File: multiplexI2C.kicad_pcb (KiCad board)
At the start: 2 copper layers, 48.3 x 71.1 mm, 58 parts, among them J1 Screw_Terminal_01x04, J10 Screw_Terminal_01x02, J2 Screw_Terminal_01x04, J3 Screw_Terminal_01x04, J4 Screw_Terminal_01x04, J5 Screw_Terminal_01x04, J6 Screw_Terminal_01x04, J7 Screw_Terminal_01x04, J8 Screw_Terminal_01x04, J9 Conn_02x04_Top_Bottom, U1 PCA9548A, U4 AMS1117-3.3 SOT-223, U5 f411-RFM95W

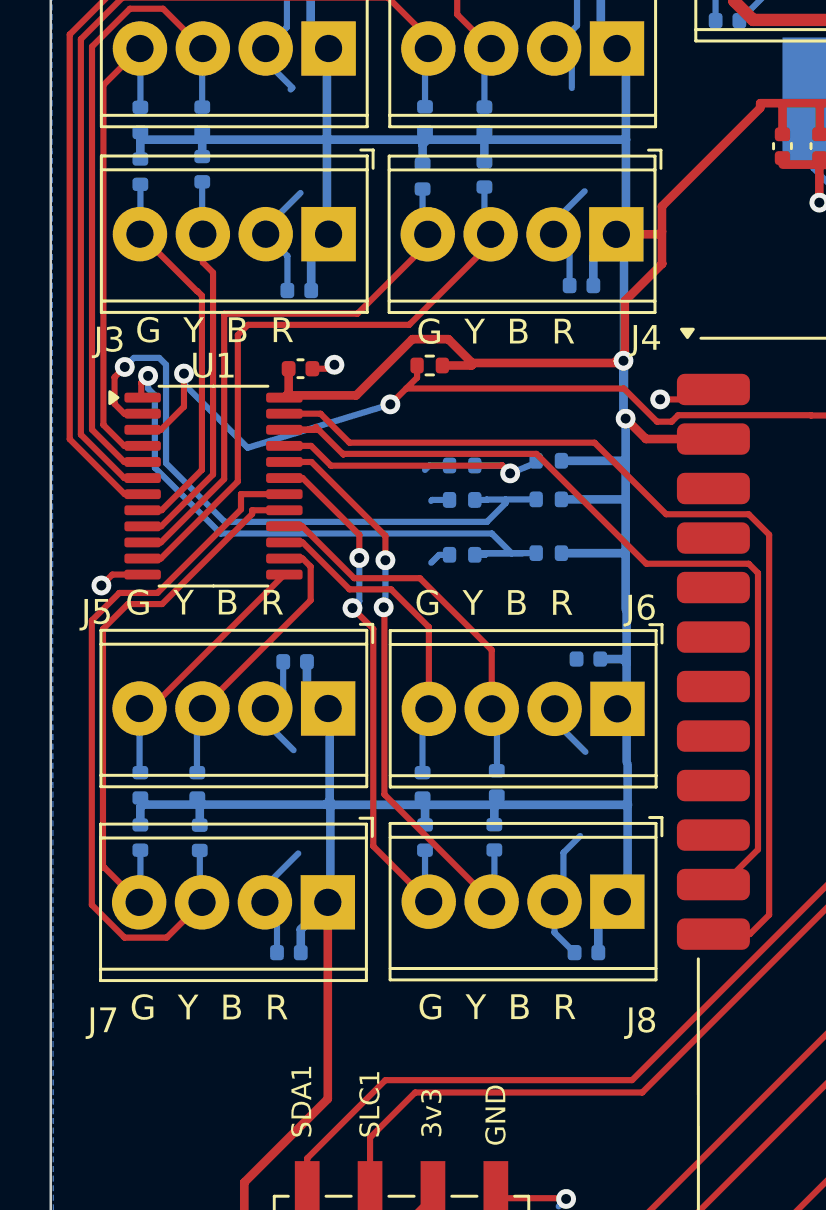
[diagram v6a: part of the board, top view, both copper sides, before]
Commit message: four sensor connectors flipped to the way they should be installed.
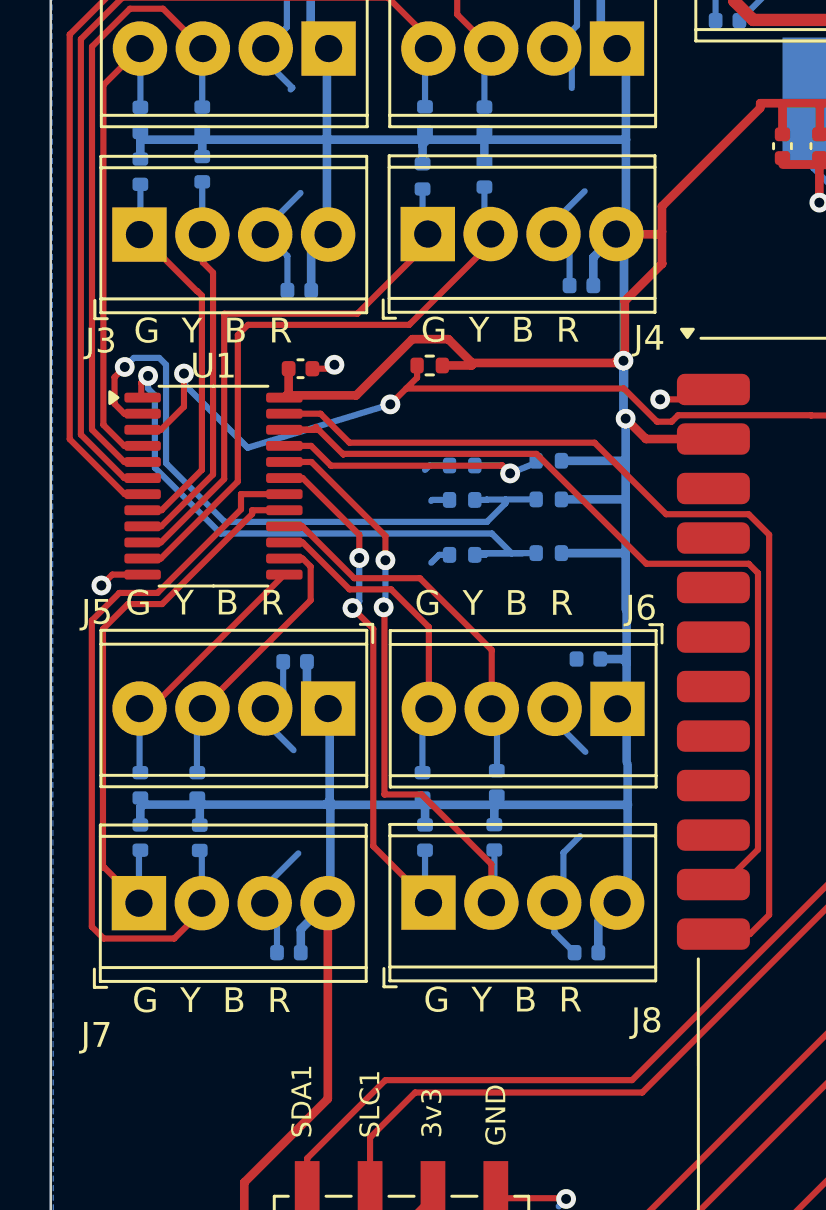
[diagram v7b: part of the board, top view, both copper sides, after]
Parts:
- moved J3 7.51 mm to (53.2, 41.0), turned to 0 degrees
- moved J8 7.50 mm to (64.9, 68.0), turned to 0 degrees
- moved J7 7.50 mm to (53.2, 68.0), turned to 0 degrees
- moved J4 7.49 mm to (64.8, 41.0), turned to 0 degrees
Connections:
- J3 pad 1: +3V3 -> /Connector_flipped2/SD
- J3 pad 2: GND -> /Connector_flipped2/SC
- J3 pad 3: /Connector2/SC -> GND
- J3 pad 4: /Connector2/SD -> +3V3
- J4 pad 1: +3V3 -> /Connector_flipped3/SD
- J4 pad 2: GND -> /Connector_flipped3/SC
- J4 pad 3: /Connector3/SC -> GND
- J4 pad 4: /Connector3/SD -> +3V3
- J7 pad 1: +3V3 -> /Connector_flipped6/SD
- J7 pad 2: GND -> /Connector_flipped6/SC
- J7 pad 3: /Connector6/SC -> GND
- J7 pad 4: /Connector6/SD -> +3V3
- J8 pad 1: +3V3 -> /Connector_flipped7/SD
- J8 pad 2: GND -> /Connector_flipped7/SC
- J8 pad 3: /Connector7/SC -> GND
- J8 pad 4: /Connector7/SD -> +3V3
- R14 pad 2: /Connector2/SC -> /Connector_flipped2/SC
- R15 pad 2: /Connector2/SD -> /Connector_flipped2/SD
- R16 pad 2: /Connector3/SC -> /Connector_flipped3/SC
- R17 pad 2: /Connector3/SD -> /Connector_flipped3/SD
- R22 pad 2: /Connector6/SC -> /Connector_flipped6/SC
- R23 pad 2: /Connector6/SD -> /Connector_flipped6/SD
- R24 pad 2: /Connector7/SC -> /Connector_flipped7/SC
- R25 pad 2: /Connector7/SD -> /Connector_flipped7/SD
- U1 pad 10: /Connector3/SD -> /Connector_flipped3/SD
- U1 pad 11: /Connector3/SC -> /Connector_flipped3/SC
- U1 pad 17: /Connector6/SD -> /Connector_flipped6/SD
- U1 pad 18: /Connector6/SC -> /Connector_flipped6/SC
- U1 pad 19: /Connector7/SD -> /Connector_flipped7/SD
- U1 pad 20: /Connector7/SC -> /Connector_flipped7/SC
- U1 pad 8: /Connector2/SD -> /Connector_flipped2/SD
- U1 pad 9: /Connector2/SC -> /Connector_flipped2/SC
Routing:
- net /Connector_flipped6/SC: track 0.00 -> 30.2 mm
- net /Connector6/SC: track 29.3 -> 0.00 mm
- net /Connector_flipped3/SC: track 0.00 -> 25.0 mm
- net /Connector3/SC: track 25.0 -> 0.00 mm
- net /Connector_flipped7/SC: track 0.00 -> 24.8 mm, vias 0 -> 2
- net /Connector7/SC: track 23.9 -> 0.00 mm, vias 2 -> 0
- net /Connector_flipped6/SD: track 0.00 -> 23.3 mm
- net /Connector6/SD: track 23.1 -> 0.00 mm
- net /Connector_flipped3/SD: track 0.00 -> 22.6 mm
- net /Connector3/SD: track 22.6 -> 0.00 mm
- net /Connector_flipped7/SD: track 0.00 -> 22.1 mm, vias 0 -> 2
- net /Connector7/SD: track 22.1 -> 0.00 mm, vias 2 -> 0
- net /Connector_flipped2/SC: track 0.00 -> 15.7 mm
- net /Connector2/SC: track 15.7 -> 0.00 mm
- net /Connector_flipped2/SD: track 0.00 -> 15.6 mm
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
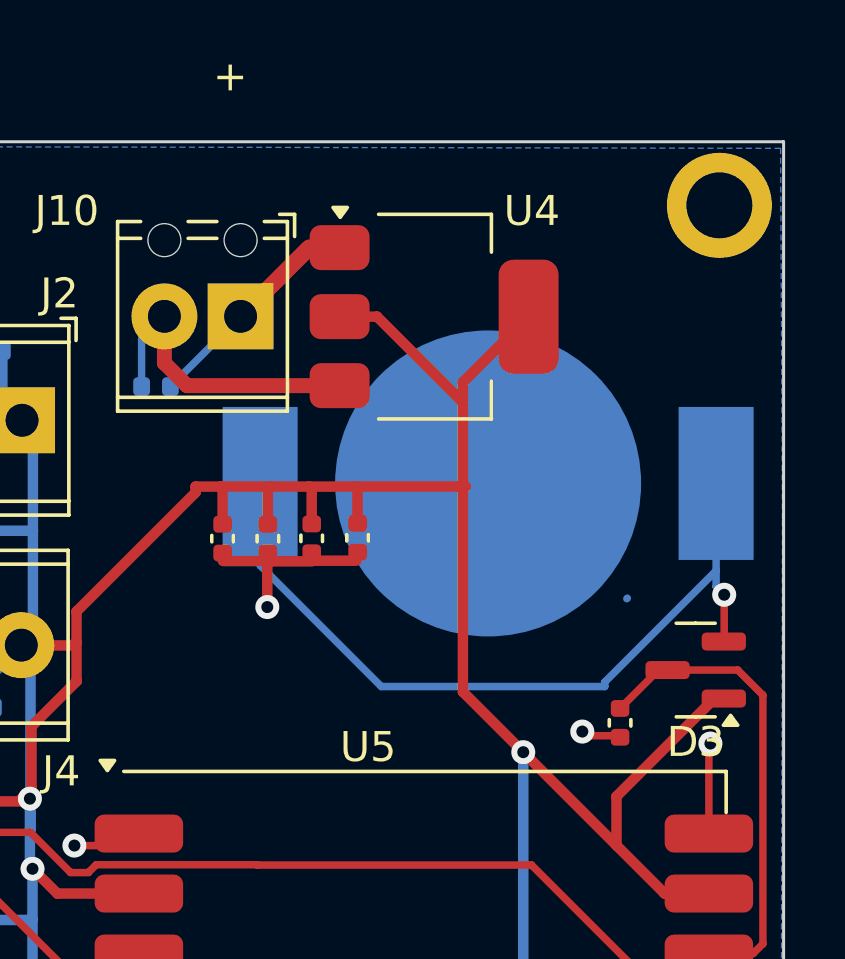
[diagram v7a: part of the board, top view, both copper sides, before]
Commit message: changed single 10k pull-up to 4.7k like others. Renumbered components to fill numbering gaps.
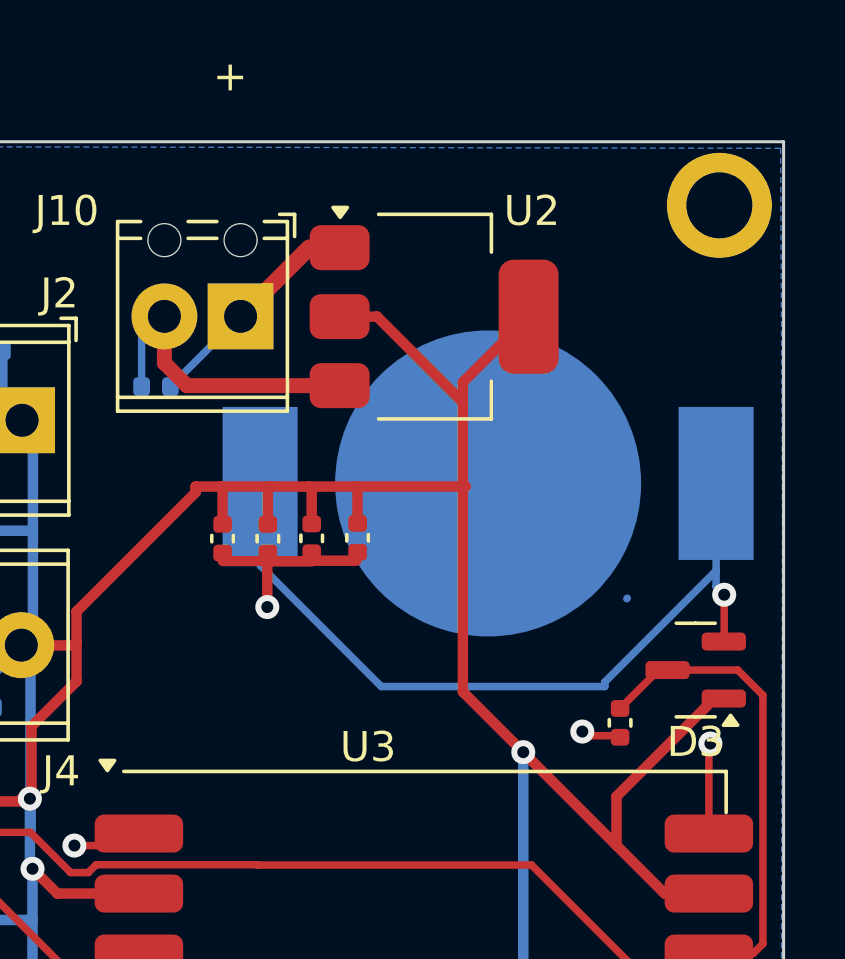
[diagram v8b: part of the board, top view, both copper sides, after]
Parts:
- R7: renamed from R9; value 10k -> 4.7k
- renumbered C17 to C10, C18 to C11, C19 to C12, C20 to C13, C21 to C14, C22 to C15, R12 to R10, R13 to R11, R14 to R12, R15 to R13, R16 to R14, R17 to R15, R18 to R16, R19 to R17, R20 to R18, R21 to R19, R22 to R20, R23 to R21, R24 to R22, R25 to R23, R10 to R8, R11 to R9, U4 to U2, U5 to U3
